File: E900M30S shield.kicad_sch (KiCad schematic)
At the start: 5 parts, among them J1 Conn10, J2 Conn02, U1 E22-900M30S

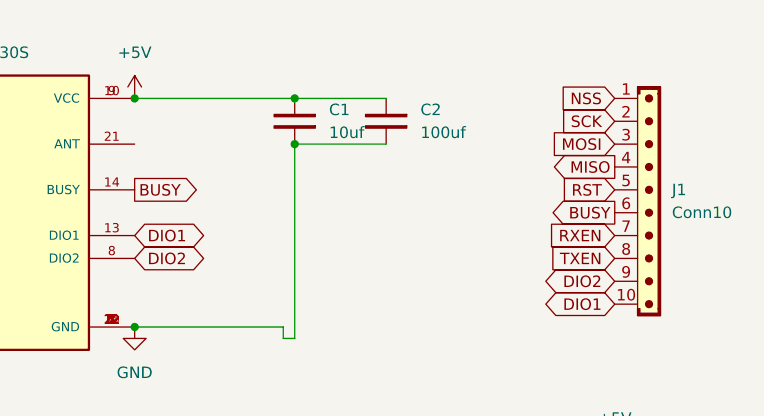
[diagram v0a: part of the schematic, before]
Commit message: Update cap values
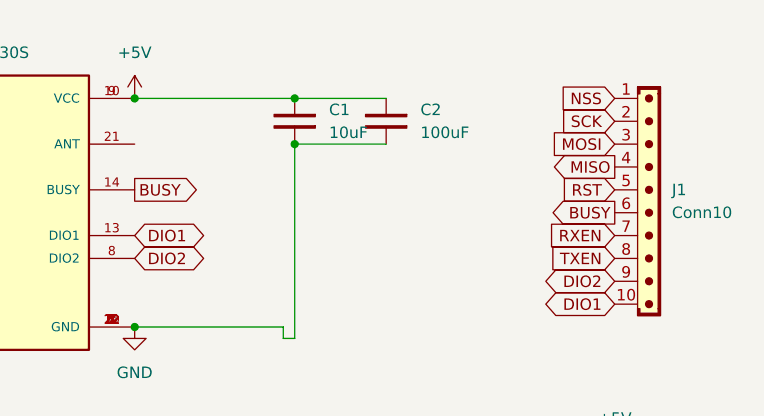
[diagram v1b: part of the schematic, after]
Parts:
- C1: value 10uf -> 10uF
- C2: value 100uf -> 100uF
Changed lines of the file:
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@@
 			)
 		)
-		(property "Value" "100uf"
+		(property "Value" "100uF"
 			(at 101.6 45.7199 90)
 			(effects
@@
 			)
 		)
-		(property "Value" "10uf"
+		(property "Value" "10uF"
 			(at 91.44 45.7199 90)
 			(effects

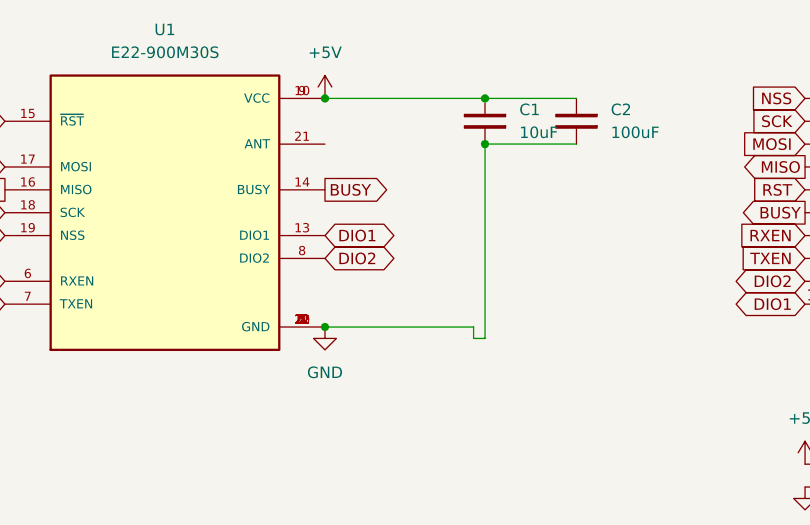
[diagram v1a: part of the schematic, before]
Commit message: Rearrange decoupling caps Front side ground plane Double width power traces
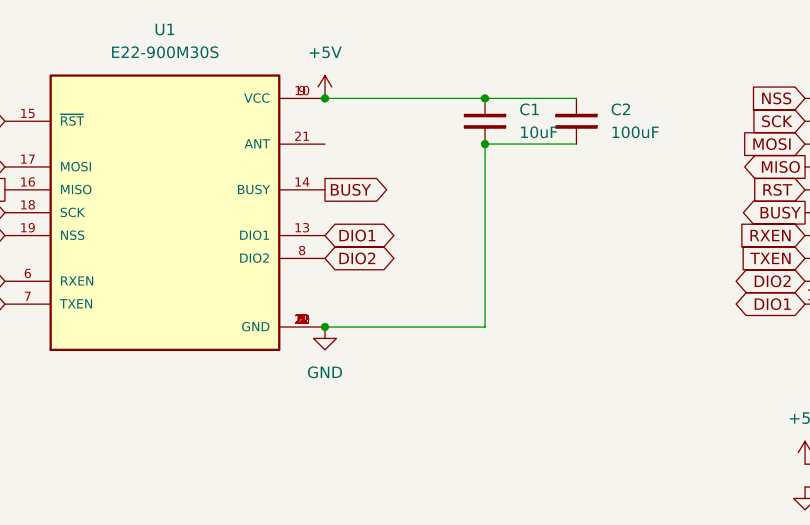
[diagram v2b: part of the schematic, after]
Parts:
- C1, C2: footprint Capacitor_SMD:C_0805_2012Metric -> Capacitor_SMD:C_1210_3225Metric
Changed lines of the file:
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@@
 	(wire
 		(pts
-			(xy 86.36 67.31) (xy 69.85 67.31)
+			(xy 69.85 67.31) (xy 87.63 67.31)
 		)
 		(stroke
@@
 	(wire
 		(pts
-			(xy 87.63 68.58) (xy 86.36 68.58)
-		)
-		(stroke
-			(width 0)
-			(type default)
-		)
-	)
-	(wire
-		(pts
-			(xy 87.63 46.99) (xy 87.63 68.58)
-		)
-		(stroke
-			(width 0)
-			(type default)
-		)
-	)
-	(wire
-		(pts
-			(xy 86.36 68.58) (xy 86.36 67.31)
+			(xy 87.63 46.99) (xy 87.63 67.31)
 		)
 		(stroke
@@
 			)
 		)
-		(property "Footprint" "Capacitor_SMD:C_0805_2012Metric"
+		(property "Footprint" "Capacitor_SMD:C_1210_3225Metric"
 			(at 93.98 44.45 0)
 			(effects
@@
 			)
 		)
-		(property "Footprint" "Capacitor_SMD:C_0805_2012Metric"
+		(property "Footprint" "Capacitor_SMD:C_1210_3225Metric"
 			(at 83.82 44.45 0)
 			(effects

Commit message: Final touches
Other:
- company: (none) -> Stefan Gofferje
- title: (none) -> Breakout board for eByte E22 SPI modules with CM4 footprint
- moved on the sheet: C1, C2, J1, J2, U1
